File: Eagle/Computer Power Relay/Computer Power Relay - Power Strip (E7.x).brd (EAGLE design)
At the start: 79.5 x 78 mm, 5 parts, among them K1 RELAY-3V3DC-110VAC012, K3 RELAY-110VACV3_IN-PLACE

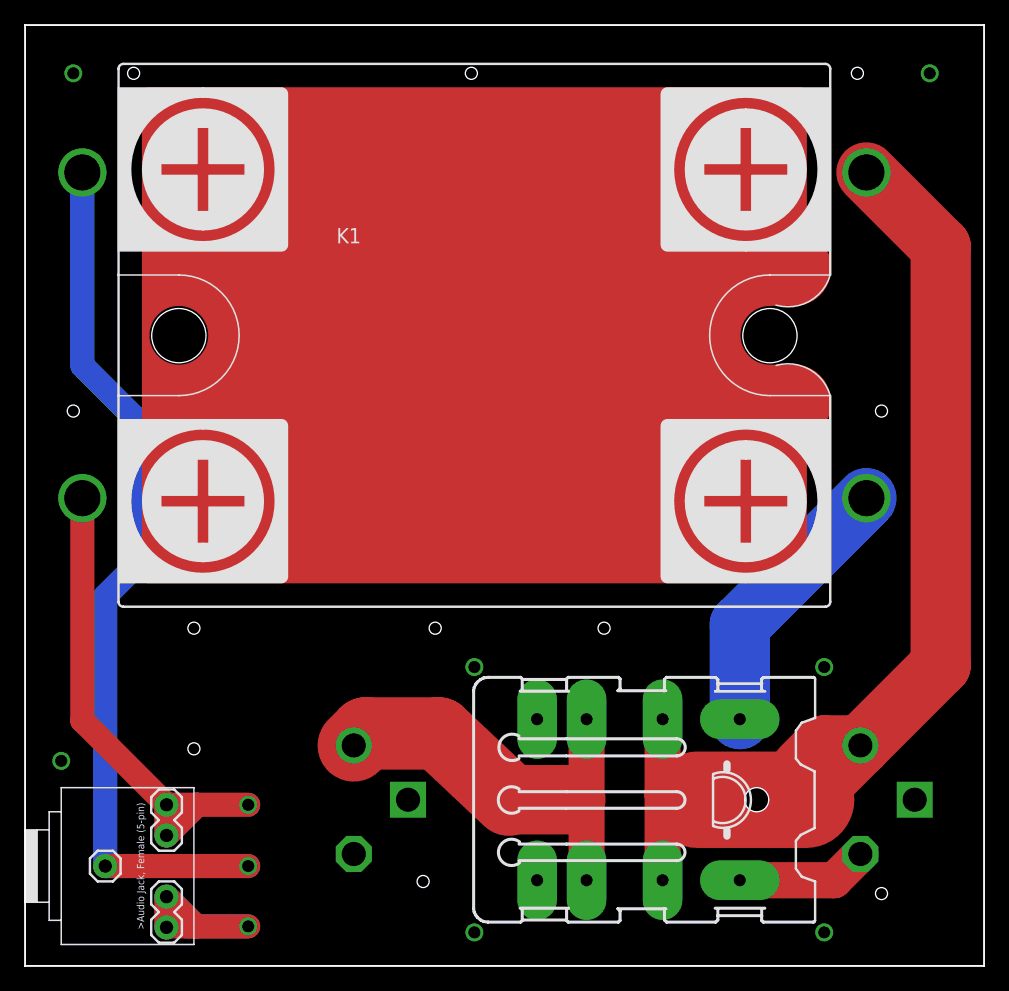
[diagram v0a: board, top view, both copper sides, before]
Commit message: Beginning Merge of Boards (Relay)
I'm beginning to merge the Controller and Power Strip boards into one so that I can print it for cheaper.
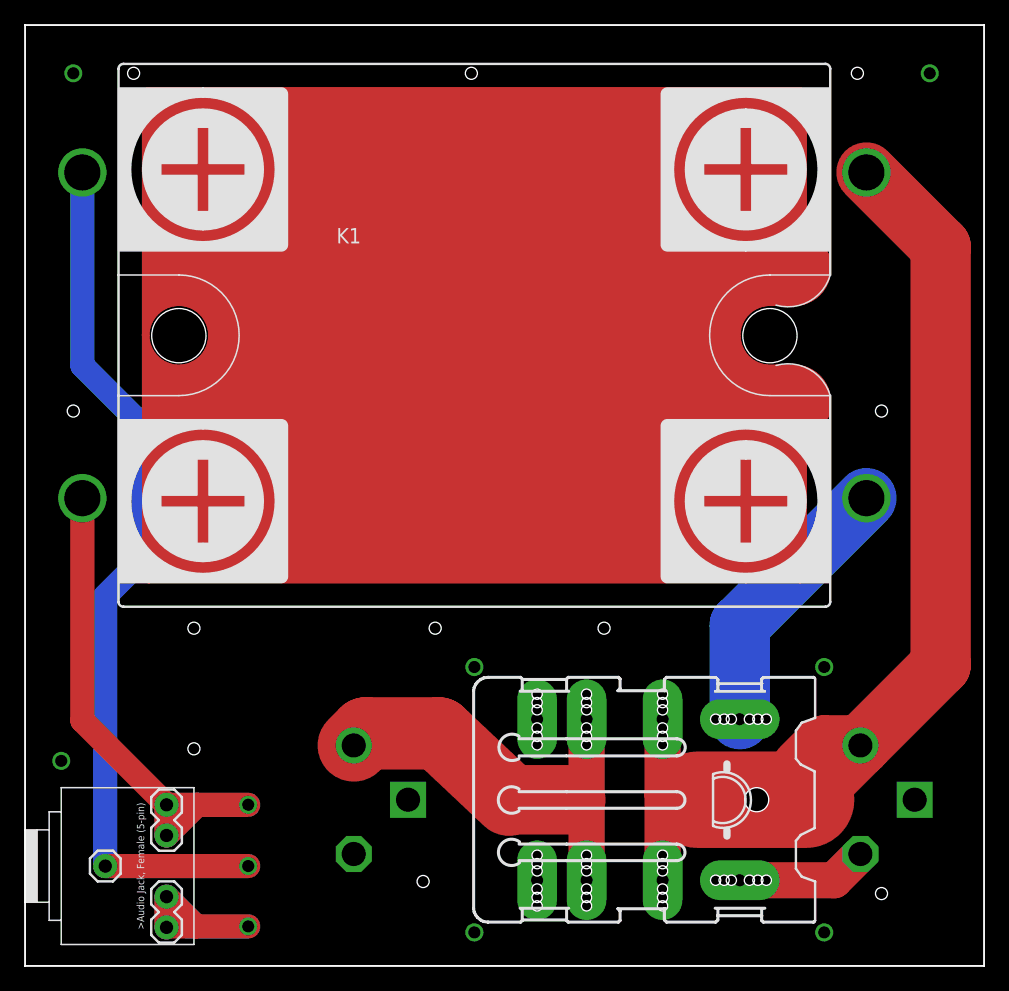
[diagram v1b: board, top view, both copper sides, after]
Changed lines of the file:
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@@
 <?xml version="1.0" encoding="utf-8"?>
 <!DOCTYPE eagle SYSTEM "eagle.dtd">
-<eagle version="9.6.2">
+<eagle version="7.7.0">
 <drawing>
 <settings>
@@
 <attribute name="VALUE" x="38.1653125" y="23.14875" size="0.6096" layer="27" rot="R270"/>
 </element>
-<element name="K1" library="Inventory" package="RELAY-3V3-110V" package3d_urn="urn:adsk.eagle:package:24461/1" value="RELAY-3V3DC-110VAC012" x="37.25" y="52.28" smashed="yes" rot="R270">
+<element name="K1" library="Inventory" package="RELAY-3V3-110V" value="RELAY-3V3DC-110VAC012" x="37.25" y="52.28" smashed="yes" rot="R270">
 <attribute name="MF" value="" x="37.25" y="52.28" size="0.6096" layer="27" rot="R270" display="off"/>
 <attribute name="MPN" value="ACV33012" x="37.25" y="52.28" size="0.6096" layer="27" rot="R270" display="off"/>
@@
 which will not be processed correctly with this version.
 </note>
-<note version="8.3" severity="warning">
-Since Version 8.3, EAGLE supports URNs for individual library
-assets (packages, symbols, and devices). The URNs of those assets
-will not be understood (or retained) with this version.
-</note>
-<note version="8.3" severity="warning">
-Since Version 8.3, EAGLE supports the association of 3D packages
-with devices in libraries, schematics, and board files. Those 3D
-packages will not be understood (or retained) with this version.
-</note>
 </compatibility>
